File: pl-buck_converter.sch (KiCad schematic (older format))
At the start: 41 parts

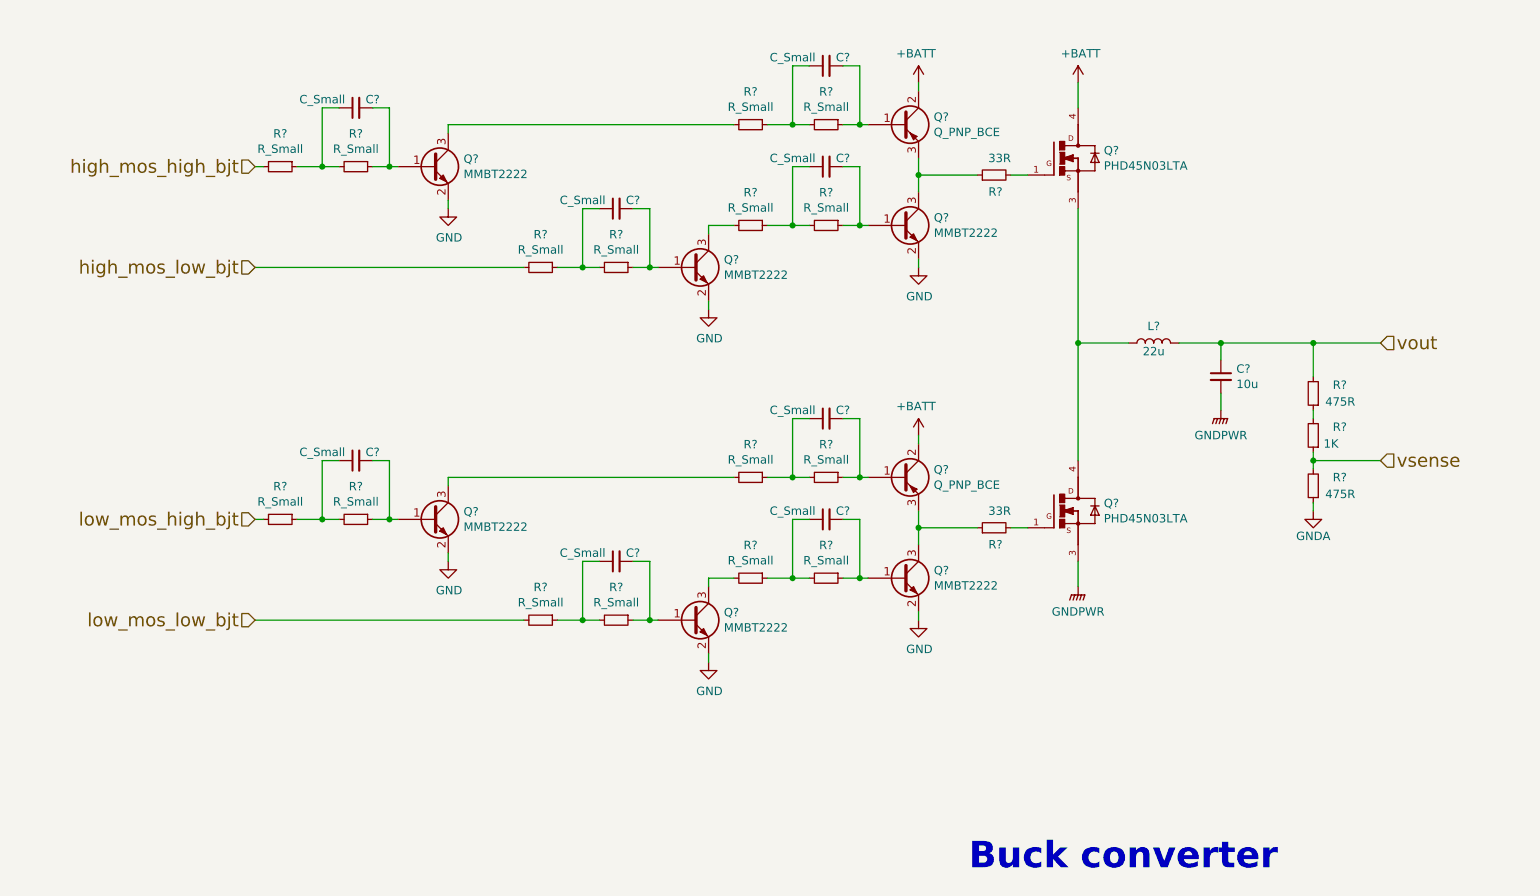
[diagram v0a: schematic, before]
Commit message: Added component values
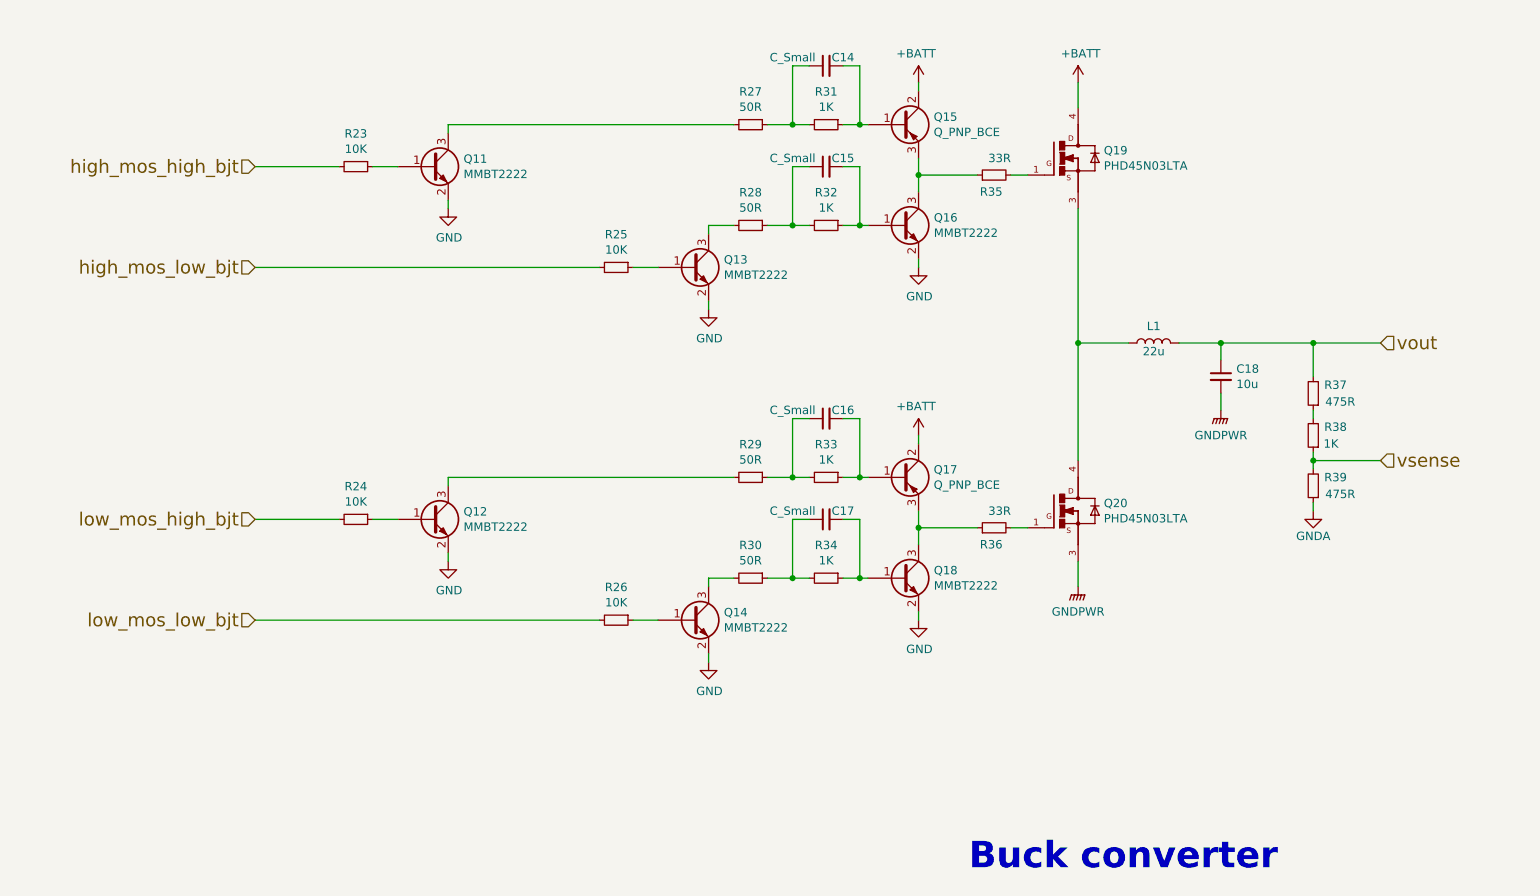
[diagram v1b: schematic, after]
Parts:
- removed C? (x4): C_Small, symbol Device:C_Small
- removed R? (x13): R_Small, symbol Device:R_Small
- added R23, R24, R25: 10K, symbol Device:R_Small
- added R28, R29, R30: 50R, symbol Device:R_Small
- added R32, R33, R34: 1K, symbol Device:R_Small
- R26: renamed from R?; value R_Small -> 10K
- R27: renamed from R?; value R_Small -> 50R
- R31: renamed from R?; value R_Small -> 1K
- gave numbers to parts that had none: 21
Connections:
- net high_mos_high_bjt: now also R23.2
- net high_mos_low_bjt: now also R25.2
- net low_mos_high_bjt: now also R24.2
- net low_mos_low_bjt: now also R26.2
- net at C15.2, Q16.1 (B): now also R32.1
- net at C15.1: now also R28.1, R32.2
- net at Q13.3 (C): now also R28.2
- net at Q11.1 (B): now also R23.1
- net at Q13.1 (B): now also R25.1
- net at C17.2, Q18.1 (B): now also R34.1
- net at C16.2, Q17.1 (B): now also R33.1
- net at C16.1: now also R29.1, R33.2
- net at Q12.3 (C): now also R29.2
- net at C17.1: now also R30.1, R34.2
- net at Q12.1 (B): now also R24.1
- net at Q14.3 (C): now also R30.2

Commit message: Schematics redesigned and fixed
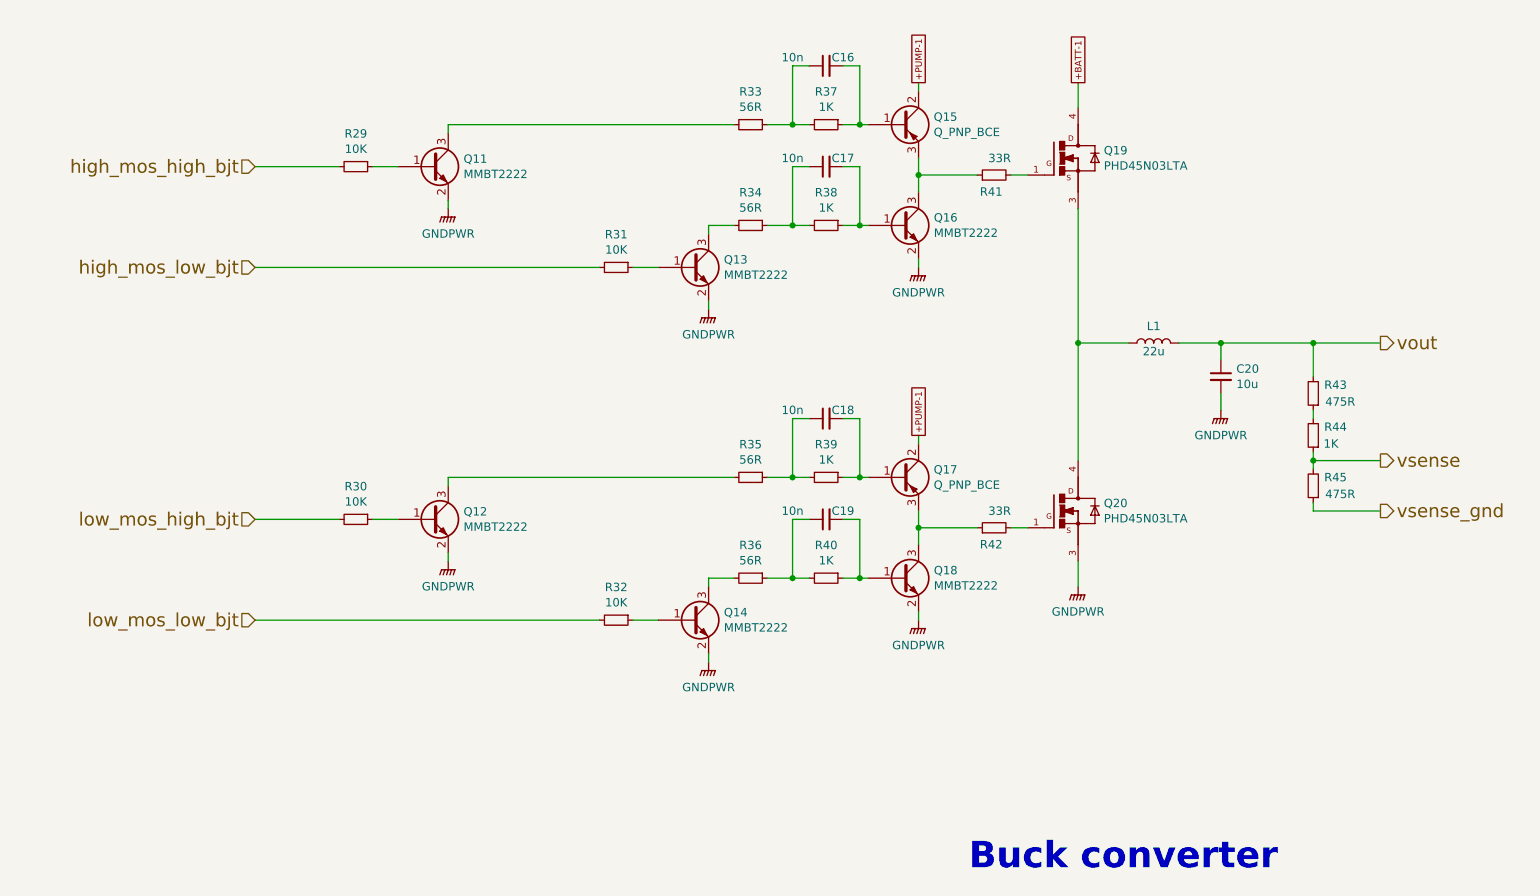
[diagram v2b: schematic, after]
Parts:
- removed C15, C16: C_Small, symbol Device:C_Small
- removed R28, R29, R30: 50R, symbol Device:R_Small
- added C18, C19: 10n, Capacitor_SMD:C_0805_2012Metric_Pad1.15x1.40mm_HandSolder, symbol Device:C_Small
- added R34, R35, R36: 56R, Resistor_SMD:R_0805_2012Metric_Pad1.15x1.40mm_HandSolder, symbol Device:R_Small
- C16: renamed from C14; value C_Small -> 10n; footprint (none) -> Capacitor_SMD:C_0805_2012Metric_Pad1.15x1.40mm_HandSolder
- C17: value C_Small -> 10n; footprint (none) -> Capacitor_SMD:C_0805_2012Metric_Pad1.15x1.40mm_HandSolder
- Q15, Q17: footprint (none) -> Package_TO_SOT_SMD:SOT-23
- R29: renamed from R23; footprint (none) -> Resistor_SMD:R_0805_2012Metric_Pad1.15x1.40mm_HandSolder
- R30: renamed from R24; footprint (none) -> Resistor_SMD:R_0805_2012Metric_Pad1.15x1.40mm_HandSolder
- R31: renamed from R25; footprint (none) -> Resistor_SMD:R_0805_2012Metric_Pad1.15x1.40mm_HandSolder
- R32: renamed from R26; footprint (none) -> Resistor_SMD:R_0805_2012Metric_Pad1.15x1.40mm_HandSolder
- R33: renamed from R27; value 50R -> 56R; footprint (none) -> Resistor_SMD:R_0805_2012Metric_Pad1.15x1.40mm_HandSolder
- R37: renamed from R31; footprint (none) -> Resistor_SMD:R_0603_1608Metric_Pad1.05x0.95mm_HandSolder
- R38: renamed from R32; footprint (none) -> Resistor_SMD:R_0603_1608Metric_Pad1.05x0.95mm_HandSolder
- R39: renamed from R33; footprint (none) -> Resistor_SMD:R_0603_1608Metric_Pad1.05x0.95mm_HandSolder
- R40: renamed from R34; footprint (none) -> Resistor_SMD:R_0603_1608Metric_Pad1.05x0.95mm_HandSolder
- renumbered C18 to C20, R35 to R41, R36 to R42, R37 to R43, R38 to R44, R39 to R45
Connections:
- net GND is gone; now on net GNDPWR: Q11.2 (E), Q12.2 (E), Q13.2 (E), Q14.2 (E), Q16.2 (E), Q18.2 (E)
- net at Q16.1 (B), R38.1: now also C17.2
- net at R38.2: now also C17.1, R34.1
- net at Q17.1 (B), R39.1: now also C18.2
- net at R39.2: now also C18.1, R35.1
- net at Q18.1 (B), R40.1: now also C19.2; no longer C17.2
- net at R40.2: now also C19.1, R36.1; no longer C17.1
- net at Q13.3 (C): now also R34.2
- net at Q12.3 (C): now also R35.2
- net at Q14.3 (C): now also R36.2
- net +BATT renamed +PUMP-1
- net +PUMP-1: no longer Q19.4
- net GNDA renamed vsense_gnd
- new net +BATT-1: Q19.4
